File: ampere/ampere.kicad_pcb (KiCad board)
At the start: 4 copper layers, 76 parts, among them J1 USB_C_Receptacle_USB2.0_16P, Q2 CSD25480F3, Q3 CSD25480F3, Q4 CSD15380F3, Q5 CSD15380F3, Q6 CSD15380F3, Q7 CSD15380F3, Q8 CSD18543Q3A, U1 LP5907MFX-3.3, U2 STM32G474RETx, U3 TPS26750SRSMR, U4 TPD4S480RUKR, U5 CAT24C256, Y1 25 MHZ, Y2 32.768 KHZ

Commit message: add LDOs, 90 percent of TPS55289s
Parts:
- removed R10, R11, R8, R9: 100K, Resistor_SMD:R_0402_1005Metric
- added C100: 100uF, Capacitor_SMD:CP_Elec_6.3x5.8, F.Cu at (-58.7, 158.9)
- added C101: 1uF, Capacitor_SMD:C_0603_1608Metric, F.Cu at (145.5, 15.4)
- added C102: 100nF, Capacitor_SMD:C_0402_1005Metric, F.Cu at (-56.4, 165.0)
- added C103: 10uF, Capacitor_SMD:C_1206_3216Metric, F.Cu at (160.0, 70.7)
- added C105: 10uF, Capacitor_SMD:C_1206_3216Metric, F.Cu at (177.5, 70.7)
- added C106: 100nF, Capacitor_SMD:C_0402_1005Metric, F.Cu at (113.0, 148.6)
- added C107: 100nF, Capacitor_SMD:C_0402_1005Metric, F.Cu at (142.8, 148.6)
- added C108: 100nF, Capacitor_SMD:C_0402_1005Metric, F.Cu at (159.8, 67.8)
- added C110: 100nF, Capacitor_SMD:C_0402_1005Metric, F.Cu at (177.2, 67.9)
- added C116: 10uF, Capacitor_Tantalum_SMD:CP_EIA-3528-21_Kemet-B, F.Cu at (154.3, 70.5)
- added C117: 10uF, Capacitor_Tantalum_SMD:CP_EIA-3528-21_Kemet-B, F.Cu at (171.8, 70.5)
- added C31: 100nF, Capacitor_SMD:C_0402_1005Metric, F.Cu at (101.7, 119.7)
- added C32: 100nF, Capacitor_SMD:C_0402_1005Metric, F.Cu at (101.7, 122.8)
- added C33: 100nF, Capacitor_SMD:C_0402_1005Metric, F.Cu at (96.3, 122.3)
- added C34: 100nF, Capacitor_SMD:C_0402_1005Metric, F.Cu at (82.8, 122.2)
- added C35: 1uF, Capacitor_SMD:C_0603_1608Metric, F.Cu at (95.1, 122.8)
- added C36: 10uF, Capacitor_SMD:C_1206_3216Metric, F.Cu at (93.1, 123.7)
- added C37: 10uF, Capacitor_SMD:C_1206_3216Metric, F.Cu at (90.6, 123.7)
- added C38: 10uF, Capacitor_SMD:C_1206_3216Metric, F.Cu at (88.1, 123.7)
- added C39: 100nF, Capacitor_SMD:C_0402_1005Metric, F.Cu at (96.8, 124.9)
- added C40: 100nF, Capacitor_SMD:C_0402_1005Metric, F.Cu at (100.6, 117.2)
- added C41: 100nF, Capacitor_SMD:C_0402_1005Metric, F.Cu at (82.8, 120.2)
- added C42: 100nF, Capacitor_SMD:C_0402_1005Metric, F.Cu at (96.3, 120.3)
- added C43: 1uF, Capacitor_SMD:C_0603_1608Metric, F.Cu at (95.1, 119.8)
- added C44: 10uF, Capacitor_SMD:C_1206_3216Metric, F.Cu at (90.6, 118.9)
- added C45: 10uF, Capacitor_SMD:C_1206_3216Metric, F.Cu at (93.1, 118.9)
- added C46: 4.7uF, Capacitor_SMD:C_0603_1608Metric, F.Cu at (101.0, 126.0)
- added C47: 10nF, Capacitor_SMD:C_0402_1005Metric, F.Cu at (97.6, 117.2)
- added C48: 4700pF, Capacitor_SMD:C_0402_1005Metric, F.Cu at (98.6, 127.8)
- added C49: 100pF, Capacitor_SMD:C_0402_1005Metric, F.Cu at (97.6, 127.8)
- added C50: 68uF, Capacitor_SMD:CP_Elec_8x10, F.Cu at (108.7, 107.5)
- added C51: 100uF, Capacitor_SMD:CP_Elec_6.3x5.8, F.Cu at (109.2, 134.4)
- added C52: 1uF, Capacitor_SMD:C_0603_1608Metric, F.Cu at (103.2, 130.3)
- added C53: 100nF, Capacitor_SMD:C_0402_1005Metric, F.Cu at (111.6, 140.5)
- added C54: 100nF, Capacitor_SMD:C_0402_1005Metric, F.Cu at (155.5, 67.4)
- added C55: 68uF, Capacitor_SMD:CP_Elec_8x10, F.Cu at (138.5, 107.5)
- added C56: 10uF, Capacitor_SMD:C_1206_3216Metric, F.Cu at (122.8, 118.9)
- added C57: 10uF, Capacitor_SMD:C_1206_3216Metric, F.Cu at (120.3, 118.9)
- added C58: 1uF, Capacitor_SMD:C_0603_1608Metric, F.Cu at (124.8, 119.8)
- added C59: 4.7uF, Capacitor_SMD:C_0603_1608Metric, F.Cu at (130.8, 126.0)
- added C60: 10nF, Capacitor_SMD:C_0402_1005Metric, F.Cu at (127.3, 117.2)
- added C61: 100nF, Capacitor_SMD:C_0402_1005Metric, F.Cu at (126.1, 120.3)
- added C62: 100nF, Capacitor_SMD:C_0402_1005Metric, F.Cu at (130.3, 117.2)
- added C63: 100nF, Capacitor_SMD:C_0402_1005Metric, F.Cu at (217.2, -17.7)
- added C64: 100nF, Capacitor_SMD:C_0402_1005Metric, F.Cu at (131.5, 119.7)
- added C65: 100nF, Capacitor_SMD:C_0402_1005Metric, F.Cu at (131.5, 122.8)
- added C66: 4700pF, Capacitor_SMD:C_0402_1005Metric, F.Cu at (128.3, 127.8)
- added C67: 100pF, Capacitor_SMD:C_0402_1005Metric, F.Cu at (127.3, 127.8)
- added C68: 100nF, Capacitor_SMD:C_0402_1005Metric, F.Cu at (217.2, -15.7)
- added C69: 100nF, Capacitor_SMD:C_0402_1005Metric, F.Cu at (126.1, 122.3)
- added C70: 100nF, Capacitor_SMD:C_0402_1005Metric, F.Cu at (126.6, 124.9)
- added C71: 1uF, Capacitor_SMD:C_0603_1608Metric, F.Cu at (124.8, 122.8)
- added C72: 10uF, Capacitor_SMD:C_1206_3216Metric, F.Cu at (122.8, 123.7)
- added C73: 10uF, Capacitor_SMD:C_1206_3216Metric, F.Cu at (120.3, 123.7)
- added C74: 100nF, Capacitor_SMD:C_0402_1005Metric, F.Cu at (173.0, 67.4)
- added C75: 10uF, Capacitor_SMD:C_1206_3216Metric, F.Cu at (117.8, 123.7)
- added C76: 100uF, Capacitor_SMD:CP_Elec_6.3x5.8, F.Cu at (139.0, 134.4)
- added C77: 1uF, Capacitor_SMD:C_0603_1608Metric, F.Cu at (145.5, 5.37)
- added C78: 100nF, Capacitor_SMD:C_0402_1005Metric, F.Cu at (141.3, 140.5)
- added C79: 68uF, Capacitor_SMD:CP_Elec_8x10, F.Cu at (-59.2, 132.0)
- added C80: 10uF, Capacitor_SMD:C_1206_3216Metric, F.Cu at (-74.9, 143.4)
- added C81: 10uF, Capacitor_SMD:C_1206_3216Metric, F.Cu at (-77.4, 143.4)
- added C82: 1uF, Capacitor_SMD:C_0603_1608Metric, F.Cu at (-72.9, 144.3)
- added C83: 4.7uF, Capacitor_SMD:C_0603_1608Metric, F.Cu at (-66.9, 150.4)
- added C84: 10nF, Capacitor_SMD:C_0402_1005Metric, F.Cu at (-70.4, 141.6)
- added C85: 100nF, Capacitor_SMD:C_0402_1005Metric, F.Cu at (-71.6, 144.8)
- added C86: 100nF, Capacitor_SMD:C_0402_1005Metric, F.Cu at (-67.4, 141.6)
- added C87: 100nF, Capacitor_SMD:C_0402_1005Metric, F.Cu at (220.1, -17.7)
- added C88: 100nF, Capacitor_SMD:C_0402_1005Metric, F.Cu at (-66.2, 144.2)
- added C89: 100nF, Capacitor_SMD:C_0402_1005Metric, F.Cu at (-66.2, 147.3)
- added C90: 4700pF, Capacitor_SMD:C_0402_1005Metric, F.Cu at (-69.4, 152.2)
- added C91: 100pF, Capacitor_SMD:C_0402_1005Metric, F.Cu at (-70.4, 152.2)
- added C92: 100nF, Capacitor_SMD:C_0402_1005Metric, F.Cu at (220.1, -15.7)
- added C93: 100nF, Capacitor_SMD:C_0402_1005Metric, F.Cu at (-71.6, 146.8)
- added C94: 100nF, Capacitor_SMD:C_0402_1005Metric, F.Cu at (-71.1, 149.4)
- added C95: 1uF, Capacitor_SMD:C_0603_1608Metric, F.Cu at (-72.9, 147.3)
- added C96: 10uF, Capacitor_SMD:C_1206_3216Metric, F.Cu at (-79.9, 148.1)
- added C97: 10uF, Capacitor_SMD:C_1206_3216Metric, F.Cu at (-77.4, 148.1)
- added C98: 100nF, Capacitor_SMD:C_0402_1005Metric, F.Cu at (-53.9, 165.0)
- added C99: 10uF, Capacitor_SMD:C_1206_3216Metric, F.Cu at (-74.9, 148.1)
- added D2: RED, LED_SMD:LED_0603_1608Metric, F.Cu at (97.2, 131.2)
- added D3: RED, LED_SMD:LED_0603_1608Metric, F.Cu at (127.0, 131.2)
- added D4: RED, LED_SMD:LED_0603_1608Metric, F.Cu at (-70.7, 155.6)
- added D5: 10V, Diode_SMD:D_SOD-323, F.Cu at (165.6, 77.0)
- added D6: SMBJ24CA, Diode_SMD:D_SMB, F.Cu at (165.0, 82.0)
- added D7: 10V, Diode_SMD:D_SOD-323, F.Cu at (183.1, 77.0)
- added D8: SMBJ24CA, Diode_SMD:D_SMB, F.Cu at (182.5, 82.0)
- added J2: Channel 1, Connector:Banana_Jack_2Pin, F.Cu at (112.5, -28.5)
- added J3: Channel 2, Connector:Banana_Jack_2Pin, F.Cu at (112.5, -16.5)
- added J4: Channel 3, Connector:Banana_Jack_2Pin, F.Cu at (112.5, -4.42)
- added L1: 4.7uH, Inductor_SMD:L_Changjiang_FXL1360, F.Cu at (109.0, 121.3)
- added L2: 4.7uH, Inductor_SMD:L_Changjiang_FXL1360, F.Cu at (138.8, 121.3)
- added L3: 4.7uH, Inductor_SMD:L_Changjiang_FXL1360, F.Cu at (-58.9, 145.8)
- added Q10: AO4485, Package_SO:SOIC-8_3.9x4.9mm_P1.27mm, F.Cu at (182.2, 72.1)
- added Q9: AO4485, Package_SO:SOIC-8_3.9x4.9mm_P1.27mm, F.Cu at (164.8, 72.1)
- added R30: 10m, Resistor_SMD:R_1206_3216Metric, F.Cu at (88.1, 128.5)
- added R31: 10, Resistor_SMD:R_0402_1005Metric, F.Cu at (95.3, 125.4)
- added R32: 10, Resistor_SMD:R_0402_1005Metric, F.Cu at (96.4, 126.5)
- added R33: 49.9K, Resistor_SMD:R_0402_1005Metric, F.Cu at (96.7, 117.2)
- added R34: 150K, Resistor_SMD:R_0402_1005Metric, F.Cu at (99.6, 127.8)
- added R35: 27.4K, Resistor_SMD:R_0402_1005Metric, F.Cu at (98.6, 125.7)
- added R36: 2.2K, Resistor_SMD:R_0603_1608Metric, F.Cu at (100.2, 131.2)
- added R37: 100K, Resistor_SMD:R_0402_1005Metric, F.Cu at (262.8, 112.1)
- added R38: 10m, Resistor_SMD:R_1206_3216Metric, F.Cu at (107.8, 140.5)
- added R39: 10, Resistor_SMD:R_0402_1005Metric, F.Cu at (110.1, 141.0)
- added R40: 10, Resistor_SMD:R_0402_1005Metric, F.Cu at (110.1, 140.1)
- added R41: 100K, Resistor_SMD:R_0402_1005Metric, F.Cu at (217.2, -29.6)
- added R42: 49.9K, Resistor_SMD:R_0402_1005Metric, F.Cu at (126.4, 117.2)
- added R43: 150K, Resistor_SMD:R_0402_1005Metric, F.Cu at (129.3, 127.8)
- added R44: 27.4K, Resistor_SMD:R_0402_1005Metric, F.Cu at (128.3, 125.7)
- added R45: 2.2K, Resistor_SMD:R_0603_1608Metric, F.Cu at (130.0, 131.2)
- added R46: 10, Resistor_SMD:R_0402_1005Metric, F.Cu at (125.1, 125.4)
- added R47: 10, Resistor_SMD:R_0402_1005Metric, F.Cu at (126.1, 126.5)
- added R48: 10m, Resistor_SMD:R_1206_3216Metric, F.Cu at (117.8, 128.5)
- added R49: 10, Resistor_SMD:R_0402_1005Metric, F.Cu at (139.8, 140.1)
- added R50: 10m, Resistor_SMD:R_1206_3216Metric, F.Cu at (137.6, 140.5)
- added R51: 10, Resistor_SMD:R_0402_1005Metric, F.Cu at (139.8, 141.0)
- added R52: 100K, Resistor_SMD:R_0402_1005Metric, F.Cu at (220.1, -29.6)
- added R53: 49.9K, Resistor_SMD:R_0402_1005Metric, F.Cu at (-71.3, 141.6)
- added R54: 150K, Resistor_SMD:R_0402_1005Metric, F.Cu at (-68.4, 152.2)
- added R55: 27.4K, Resistor_SMD:R_0402_1005Metric, F.Cu at (-69.4, 150.1)
- added R56: 2.2K, Resistor_SMD:R_0603_1608Metric, F.Cu at (-67.7, 155.6)
- added R57: 10, Resistor_SMD:R_0402_1005Metric, F.Cu at (-72.6, 149.9)
- added R58: 10, Resistor_SMD:R_0402_1005Metric, F.Cu at (-71.6, 150.9)
- added R59: 10m, Resistor_SMD:R_1206_3216Metric, F.Cu at (-79.9, 153.0)
- added R60: 10, Resistor_SMD:R_0402_1005Metric, F.Cu at (-57.9, 164.5)
- added R61: 10m, Resistor_SMD:R_1206_3216Metric, F.Cu at (-60.1, 165.0)
- added R62: 10, Resistor_SMD:R_0402_1005Metric, F.Cu at (-57.9, 165.5)
- added R63: 9.2K, Resistor_SMD:R_0603_1608Metric, F.Cu at (151.7, 76.3)
- added R64: 1K, Resistor_SMD:R_0603_1608Metric, F.Cu at (151.7, 73.2)
- added R65: 1.56K, Resistor_SMD:R_0603_1608Metric, F.Cu at (151.7, 69.9)
- added R66: 10K, Capacitor_SMD:C_0402_1005Metric, F.Cu at (161.8, 77.0)
- added R67: 10m, Resistor_SMD:R_1206_3216Metric, F.Cu at (157.3, 70.7)
- added R68: 9.2K, Resistor_SMD:R_0603_1608Metric, F.Cu at (169.2, 76.3)
- added R69: 1K, Resistor_SMD:R_0603_1608Metric, F.Cu at (169.2, 73.2)
- added R70: 1.56K, Resistor_SMD:R_0603_1608Metric, F.Cu at (169.2, 69.9)
- added R71: 10m, Resistor_SMD:R_1206_3216Metric, F.Cu at (174.8, 70.7)
- added R72: 10K, Resistor_SMD:R_0402_1005Metric, F.Cu at (179.3, 77.0)
- added TH1: Thermistor, Resistor_SMD:R_0603_1608Metric, F.Cu at (149.5, 2.86)
- added TH2: Thermistor, Resistor_SMD:R_0603_1608Metric, F.Cu at (149.5, 5.37)
- added TH3: Thermistor, Resistor_SMD:R_0603_1608Metric, F.Cu at (149.5, 7.88)
- added U10: TPS55289, TPS552892RYQR:CONV_TPS552892RYQR, F.Cu at (-68.9, 145.8)
- added U11: MCP4725xxx-xCH, Package_TO_SOT_SMD:SOT-23-6, F.Cu at (152.9, 65.7)
- added U12: INA238, Package_SO:TSSOP-10_3x3mm_P0.5mm, F.Cu at (-54.9, 169.4)
- added U13: INA238, Package_SO:TSSOP-10_3x3mm_P0.5mm, F.Cu at (113.8, 144.9)
- added U14: INA238, Package_SO:TSSOP-10_3x3mm_P0.5mm, F.Cu at (143.6, 144.9)
- added U15: MCP4725xxx-xCH, Package_TO_SOT_SMD:SOT-23-6, F.Cu at (170.4, 65.7)
- added U18: INA238, Package_SO:TSSOP-10_3x3mm_P0.5mm, F.Cu at (158.4, 65.4)
- added U19: INA238, Package_SO:TSSOP-10_3x3mm_P0.5mm, F.Cu at (175.9, 65.4)
- added U6: TPS55289, TPS552892RYQR:CONV_TPS552892RYQR, F.Cu at (99.1, 121.3)
- added U7: MIC29302WU, MIC29302WU:TO-263-5_ET_DDPAK_MCH, F.Cu at (156.9, 83.5)
- added U8: TPS55289, TPS552892RYQR:CONV_TPS552892RYQR, F.Cu at (128.8, 121.3)
- added U9: MIC29302WU, MIC29302WU:TO-263-5_ET_DDPAK_MCH, F.Cu at (174.4, 83.5)
- Q2, Q3: value CSD25480F3 -> CSD25481F4; footprint Package_DFN_QFN:Texas_PicoStar_DFN-3_0.69x0.60mm -> CSD25481F4:TRANS_CSD25481F4
- Q4, Q5, Q6, Q7: value CSD15380F3 -> CSD13381F4; footprint Package_DFN_QFN:Texas_PicoStar_DFN-3_0.69x0.60mm -> CSD13381F4:DFN100X60X35-3N
- moved U3 202.5 mm to (231.4, 60.3), turned to 0 degrees
- moved U5 198.0 mm to (218.6, 57.5), turned to 0 degrees
- moved J1 189.7 mm to (228.8, 52.4)
- moved Q8 188.5 mm to (231.8, 42.6)
- moved C23 186.9 mm to (218.7, 46.6), turned to 0 degrees
- moved C22 185.2 mm to (218.7, 44.6), turned to 0 degrees
- moved C26 185.0 mm to (221.6, 40.7), turned to 0 degrees
- moved C25 184.5 mm to (221.6, 38.7), turned to 0 degrees
- moved C29 183.3 mm to (221.6, 46.6)
- moved C27 181.9 mm to (221.6, 42.6)
- moved R15 180.3 mm to (207.1, 44.7), turned to 0 degrees
- moved U4 180.2 mm to (209.9, 52.0), turned to 0 degrees
- moved R27 180.0 mm to (212.9, 40.7), turned to 0 degrees
- moved C10 179.0 mm to (218.7, 42.6)
- moved R6 178.6 mm to (204.2, 48.7), turned to 0 degrees
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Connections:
- net VDD renamed MCU_VDD
- C3 pad 1: /VBUS_C -> VBUS_C
- C4 pad 1: /VBUS_C -> VBUS_C
- C5 pad 1: /VBUS_C -> VBUS_C
- C6 pad 1: /VBUS_C -> VBUS_C
- C7 pad 1: /VBUS_C -> VBUS_C
- FB1 pad 2: /VBUS_C -> VBUS_C
- U2 pad 10: unconnected-(U2-PC2-Pad10) -> TEMP_CH3
- U2 pad 12: unconnected-(U2-PA0-Pad12) -> VOLTAGE_CH1
- U2 pad 13: unconnected-(U2-PA1-Pad13) -> VOLTAGE_CH2
- U2 pad 14: unconnected-(U2-PA2-Pad14) -> VOLTAGE_CH3
- U2 pad 17: unconnected-(U2-PA3-Pad17) -> NUMPAD_ROW1
- U2 pad 18: unconnected-(U2-PA4-Pad18) -> NUMPAD_ROW2
- U2 pad 19: unconnected-(U2-PA5-Pad19) -> NUMPAD_ROW3
- U2 pad 20: unconnected-(U2-PA6-Pad20) -> NUMPAD_COL1
- U2 pad 21: unconnected-(U2-PA7-Pad21) -> NUMPAD_COL2
- U2 pad 22: unconnected-(U2-PC4-Pad22) -> NUMPAD_COL3
- U2 pad 23: unconnected-(U2-PC5-Pad23) -> NUMPAD_COL4
- U2 pad 24: unconnected-(U2-PB0-Pad24) -> NUMPAD_COL5
- U2 pad 25: unconnected-(U2-PB1-Pad25) -> NUMPAD_COL6
- U2 pad 26: unconnected-(U2-PB2-Pad26) -> NUMPAD_COL7
- U2 pad 28: unconnected-(U2-VREF+-Pad28) -> VREF+
- U2 pad 34: unconnected-(U2-PB12-Pad34) -> SD_NSS
- U2 pad 35: unconnected-(U2-PB13-Pad35) -> SD_SCK
- U2 pad 36: unconnected-(U2-PB14-Pad36) -> SD_MISO
- U2 pad 37: unconnected-(U2-PB15-Pad37) -> SD_MOSI
- U2 pad 38: unconnected-(U2-PC6-Pad38) -> CH3_SCL
- U2 pad 39: unconnected-(U2-PC7-Pad39) -> CH3_SDA
- U2 pad 40: unconnected-(U2-PC8-Pad40) -> CH2_SCL
- U2 pad 41: unconnected-(U2-PC9-Pad41) -> CH2_SDA
- U2 pad 42: unconnected-(U2-PA8-Pad42) -> CH1_SDA
- U2 pad 43: unconnected-(U2-PA9-Pad43) -> CH1_SCL
- U2 pad 49: unconnected-(U2-PA13-Pad49) -> DEBUG_SWDIO
- U2 pad 50: unconnected-(U2-PA14-Pad50) -> DEBUG_SWCLK
- U2 pad 55: unconnected-(U2-PD2-Pad55) -> DISPLAY_NSS
- U2 pad 56: unconnected-(U2-PB3-Pad56) -> DISPLAY_SCK
- U2 pad 57: unconnected-(U2-PB4-Pad57) -> DISPLAY_MISO
- U2 pad 58: unconnected-(U2-PB5-Pad58) -> DISPLAY_MOSI
- U2 pad 59: unconnected-(U2-PB6-Pad59) -> ENC1
- U2 pad 60: unconnected-(U2-PB7-Pad60) -> ENC2
- U2 pad 7: VREF+ -> unconnected-(U2-PG10-Pad7)
- U2 pad 8: unconnected-(U2-PC0-Pad8) -> TEMP_CH1
- U2 pad 9: unconnected-(U2-PC1-Pad9) -> TEMP_CH2
- U3 pad 2: ADCIN1 -> GND
- U3 pad 3: ADCIN2 -> GND
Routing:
- net CH3_SCL: track 0.00 -> 70.4 mm, vias 0 -> 2
- net CH3_SDA: track 0.00 -> 70.3 mm, vias 0 -> 3
- net CH1_SCL: track 0.00 -> 67.5 mm, vias 0 -> 3
- net CH1_SDA: track 0.00 -> 66.2 mm, vias 0 -> 3
- net CH2_SDA: track 0.00 -> 62.9 mm, vias 0 -> 3
- net CH2_SCL: track 0.00 -> 60.9 mm, vias 0 -> 3
- net /MODE: track 0.00 -> 49.9 mm, vias 0 -> 3
- net /SENSE1+: track 0.00 -> 19.8 mm
- net /SENSE2+: track 0.00 -> 19.8 mm, vias 0 -> 12
- net CH2_EN: track 0.00 -> 16.6 mm, vias 0 -> 1
- net CH1_EN: track 0.00 -> 16.6 mm, vias 0 -> 1
- net CH3_EN: track 0.00 -> 16.6 mm, vias 0 -> 1
- net /SENSE2-: track 0.00 -> 16.0 mm, vias 0 -> 7
- net /SENSE1-: track 0.00 -> 16.0 mm, vias 0 -> 7
- net 5V_VCC: track 0.00 -> 13.5 mm
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- added copper zone on F.Cu, net /SENSE1+
- added copper zone on F.Cu, net /SENSE1-
- added copper zone on F.Cu, net /SENSE2+
- added copper zone on In2.Cu, net /SENSE2+
- added copper zone on F.Cu, net /SENSE2-
- added copper zone on In2.Cu, net /SENSE2-
- added copper zone on F.Cu, net 5V_VCC
- added copper zone on B.Cu, net GND
- added copper zone on F.Cu, net GND
- added copper zone on In1.Cu, net GND
- added copper zone on In2.Cu, net GND
- added copper zone on F.Cu, net LDO1_VOUT
- added copper zone on In2.Cu, net LDO2_VOUT
- added copper zone on F.Cu, net LDO_VIN
- added copper zone on In2.Cu, net LDO_VIN
- added copper zone on F.Cu, net Net-(C51-Pad1)
- added copper zone on F.Cu, net Net-(J2-Pin_1)
- added copper zone on F.Cu, net Net-(U6-SW1)
- added copper zone on F.Cu, net Net-(U6-SW2)
- added copper zone on F.Cu, net Net-(U6-VOUT)
- added copper zone on F.Cu, net VIN
- removed copper zone on F.Cu, net /VBUS_C
- removed copper zone on F.Cu, net PP5V
- removed copper zone on F.Cu, net VBUS
- removed copper zone on F.Cu, net VBUS_LV
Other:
- board outline added: 100 x 50 mm

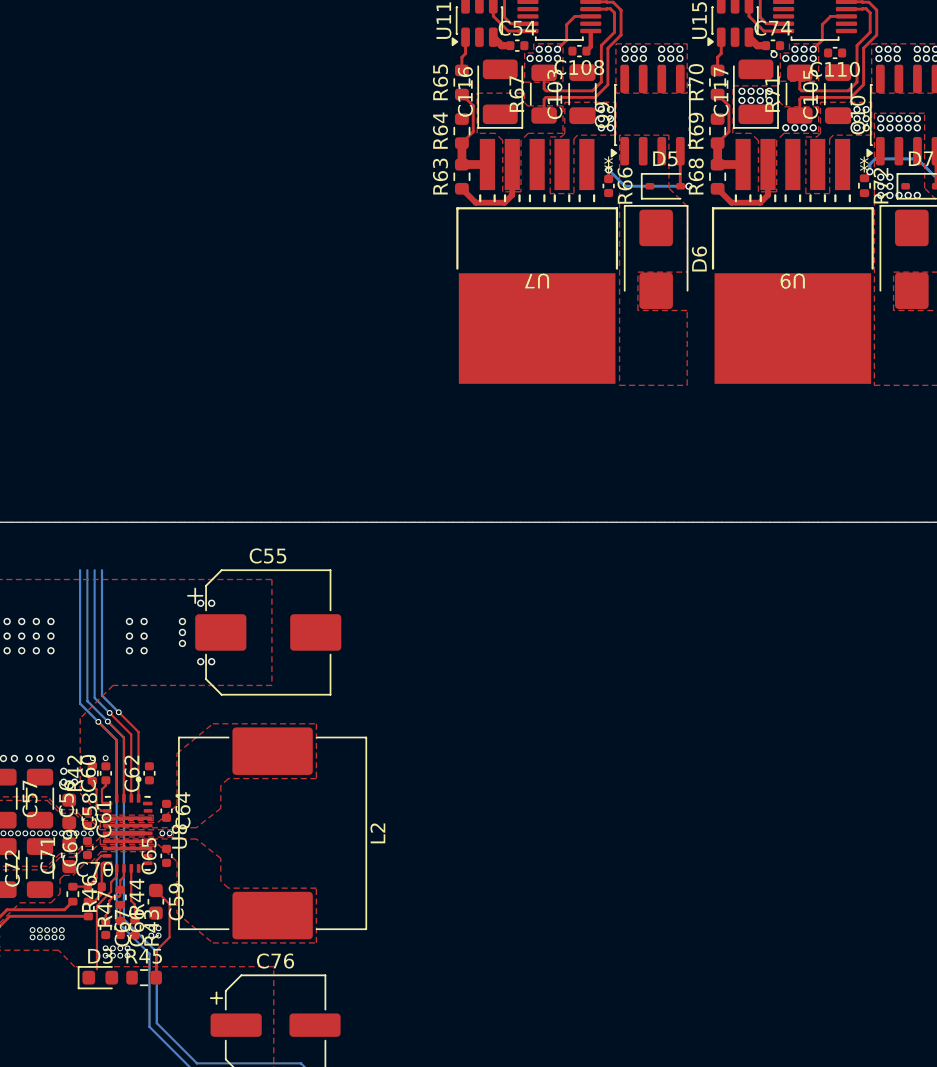
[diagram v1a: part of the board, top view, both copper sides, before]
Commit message: unified ldo input, complete 2 units for pwr pours
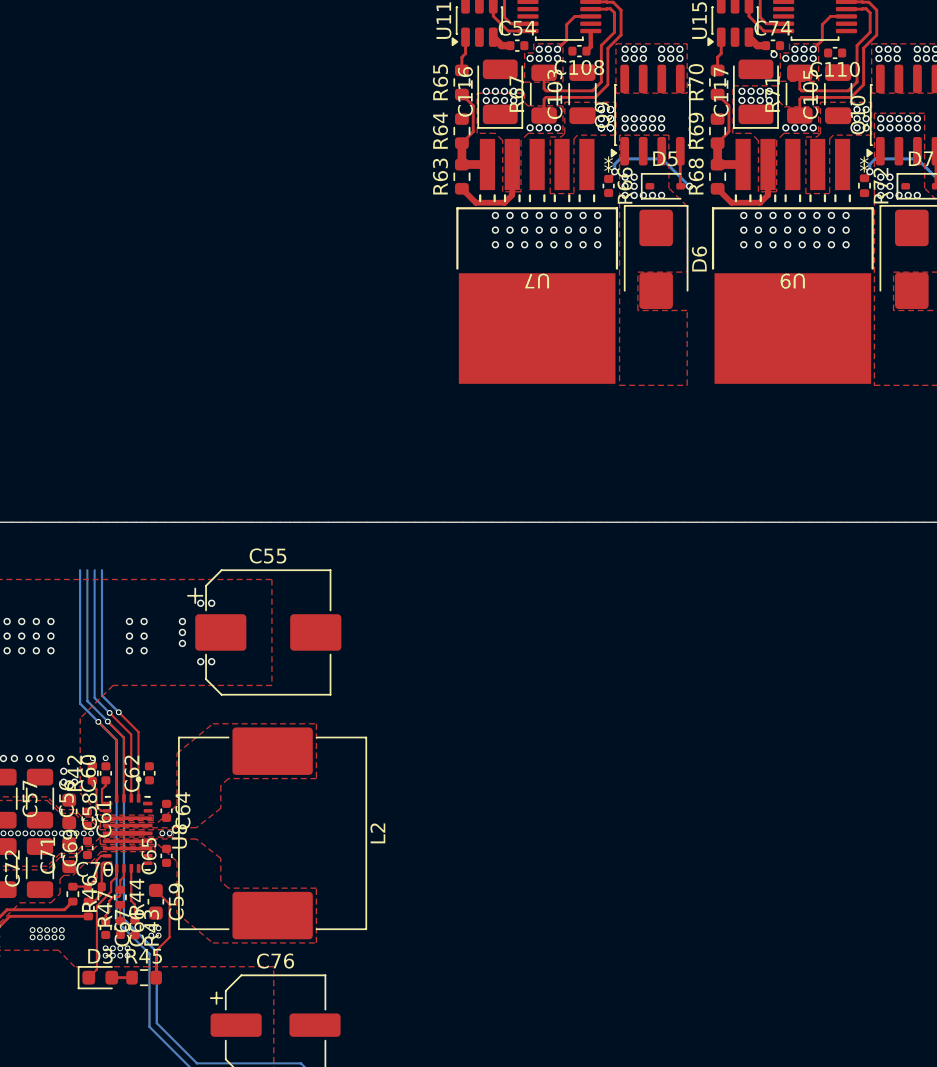
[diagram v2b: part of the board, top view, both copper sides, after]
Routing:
- net Net-(D3-A): track 0.00 -> 1.39 mm
- net Net-(D3-K): track 7.46 -> 8.27 mm
- net LDO_VIN: vias 0 -> 65
- net LDO2_VOUT: vias 0 -> 19
- net LDO1_VOUT: vias 0 -> 19
- net /SENSE2-: vias 7 -> 19
- net /SENSE2+: vias 12 -> 24
- net /SENSE1-: vias 7 -> 19
- net (no net): vias 55 -> 0
